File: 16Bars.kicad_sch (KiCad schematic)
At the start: 18 parts, among them J1 3.5mm_Mono_Switched, J2 Conn_02x05_Odd_Even, SW1 SW_Push_LED_Thonk_Low_Profile, SW2 SW_SPDT-EG1249, SW3 SW_SPDT-EG1249

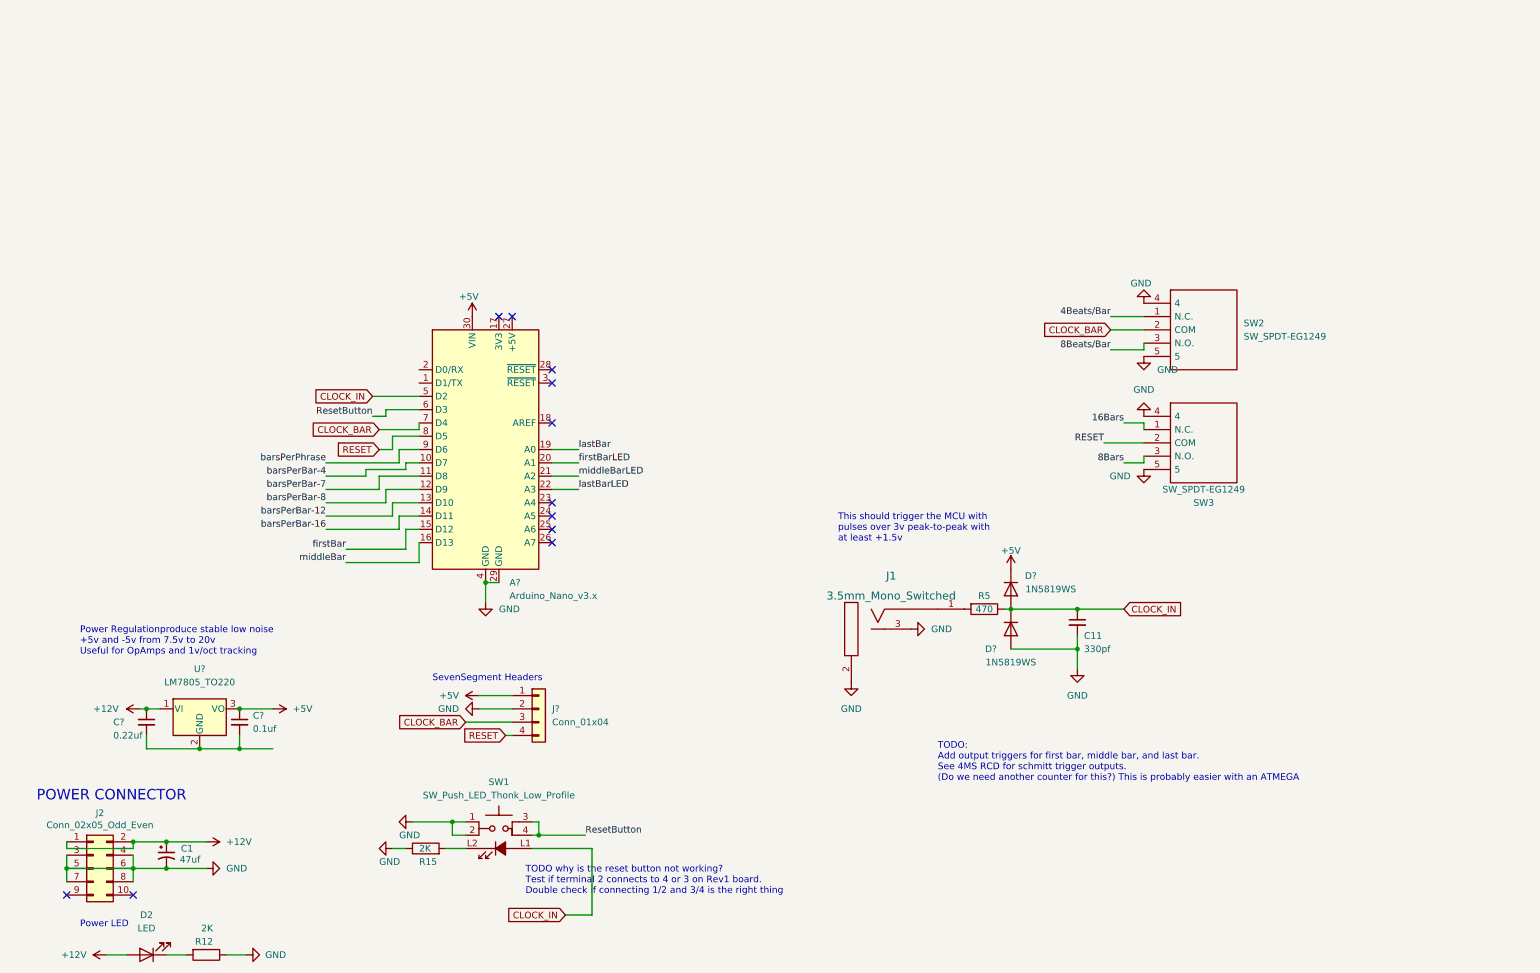
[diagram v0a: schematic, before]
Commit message: Add LCSC power regulator. Add SLB1570 5 position switch.
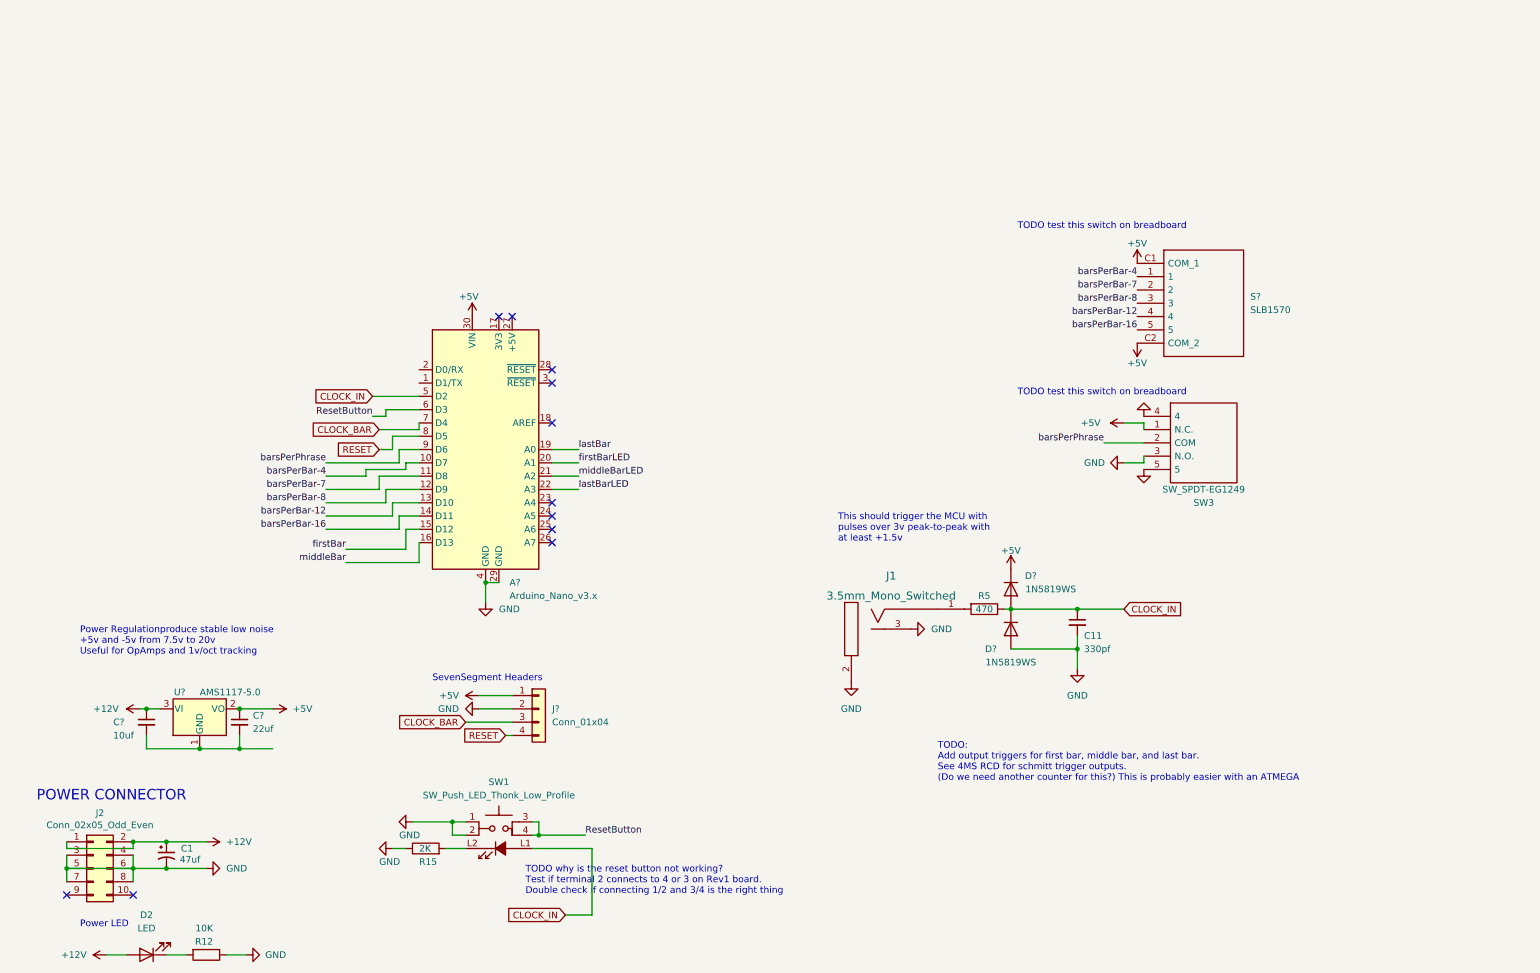
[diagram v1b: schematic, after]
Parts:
- removed SW2: SW_SPDT-EG1249, EG1249, symbol SamacSys_Parts:EG1249-On-On
- added S?: SLB1570, SLB1570, symbol SLB1570:SLB1570
- C?: value 0.1uf -> 22uf
- C?: value 0.22uf -> 10uf
- R12: value 2K -> 10K
- U?: value LM7805_TO220 -> AMS1117-5.0; footprint Package_TO_SOT_THT:TO-220-3_Vertical -> Package_TO_SOT_SMD:SOT-223-3_TabPin2; symbol Regulator_Linear:LM7805_TO220 -> Regulator_Linear:AMS1117-5.0; LCSC (none) -> C6187
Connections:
- net 16Bars is gone; now on net +5V: SW3.1 (N.C.)
- net 8Bars is gone; now on net GND: SW3.3 (N.O.)
- net +12V: now also U?.3 (VI); no longer U?.1 (VI)
- net +5V: now also U?.2 (VO), S?.C1 (COM_1), S?.C2 (COM_2); no longer U?.3 (VO)
- net RESET: no longer SW3.2 (COM)
- net barsPerBar-12: now also S?.4
- net barsPerBar-16: now also S?.5
- net barsPerBar-4: now also S?.1
- net barsPerBar-7: now also S?.2
- net barsPerBar-8: now also S?.3
- net barsPerPhrase: now also SW3.2 (COM)
- net at C?.2, C?.2: now also U?.1 (GND); no longer U?.2 (GND)
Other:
- note added: "TODO test this switch on breadboard"

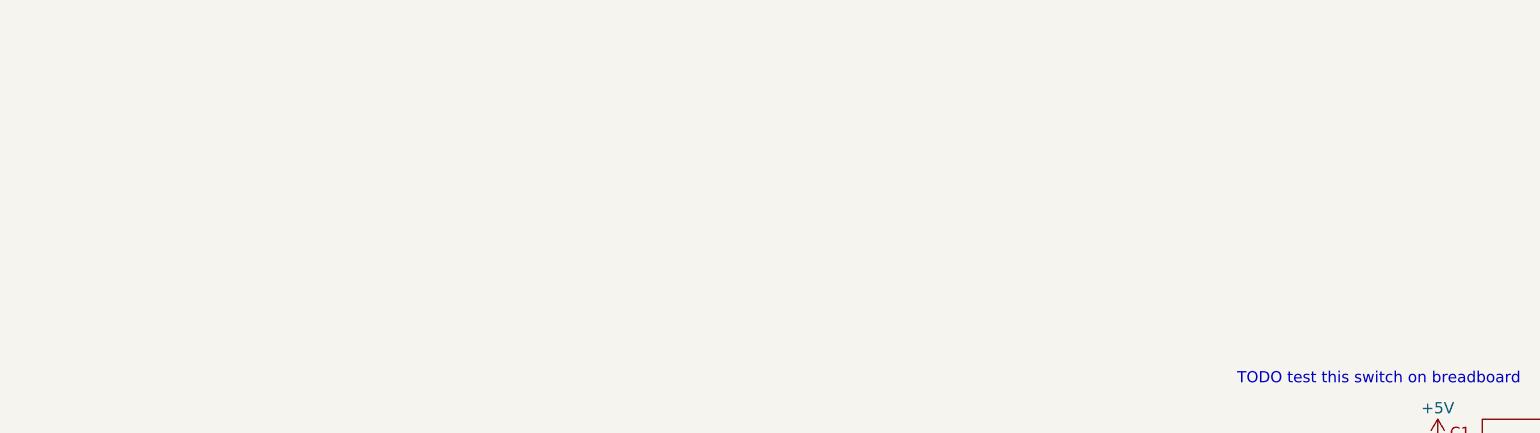
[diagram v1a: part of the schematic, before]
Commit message: Add output jacks and leds.
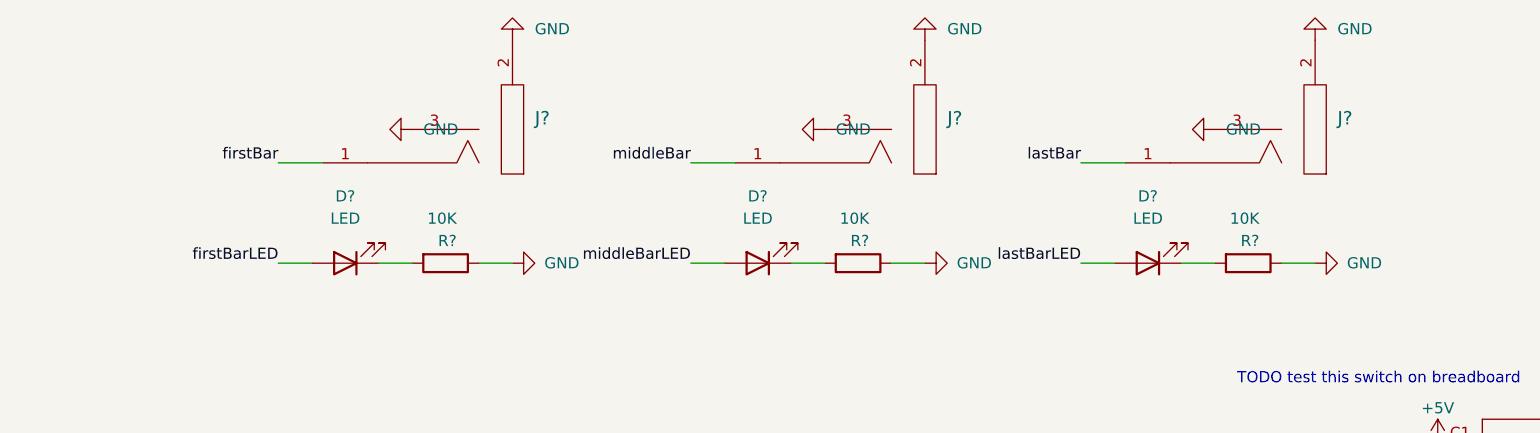
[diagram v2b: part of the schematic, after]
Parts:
- added D? (x3): LED, LED_SMD:LED_0603_1608Metric, symbol Device:LED
- added J? (x3): 3.5mm_Mono_Switched, 4ms_Jack:EighthInch_PJ398SM, symbol 4ms_Jack:3.5mm_Mono_Switched
- added R? (x3): 10K, Resistor_SMD:R_0402_1005Metric, symbol Device:R
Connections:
- net GND: now also J?.2 (SHEILD), J?.2 (SHEILD), J?.2 (SHEILD), J?.3 (SW), J?.3 (SW), J?.3 (SW), R?.1, R?.1, R?.1
- net firstBar: now also J?.1 (SIG)
- net firstBarLED: now also D?.2 (A)
- net lastBar: now also J?.1 (SIG)
- net lastBarLED: now also D?.2 (A)
- net middleBar: now also J?.1 (SIG)
- net middleBarLED: now also D?.2 (A)
- new net: D?.1 (K), R?.2 (x3)

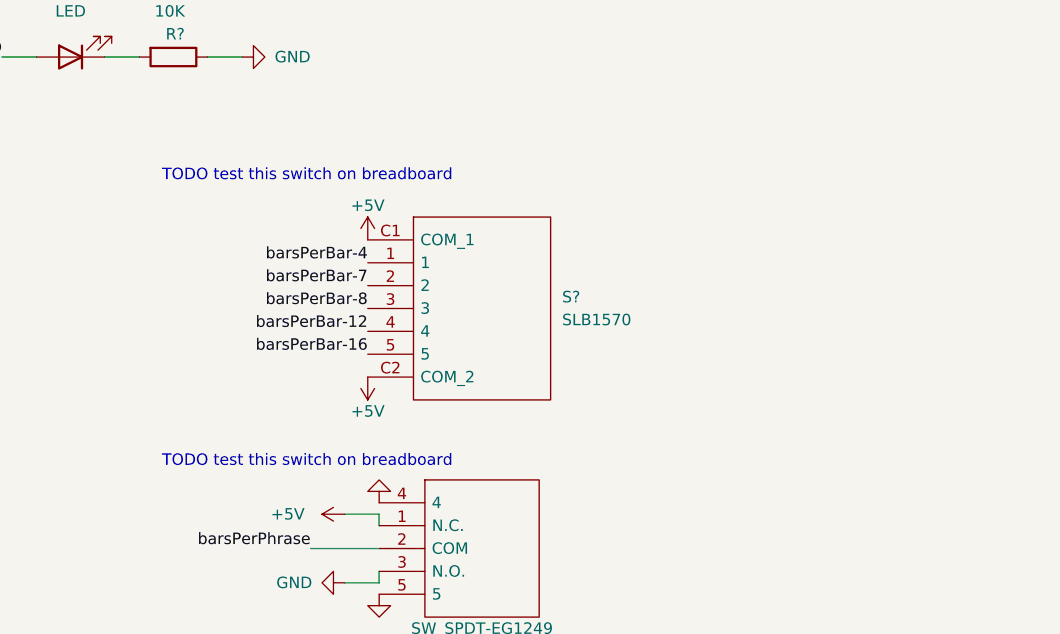
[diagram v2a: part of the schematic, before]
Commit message: Verified 1P5T Switch on Breadboard.
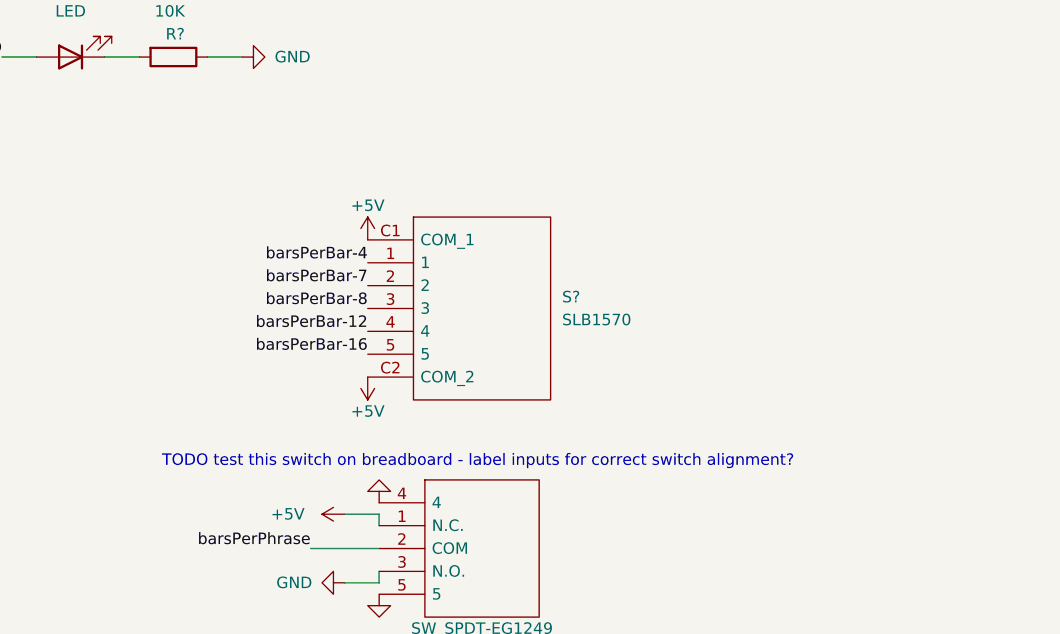
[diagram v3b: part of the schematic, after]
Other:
- note added: "TODO test this switch on breadboard - label inputs for correct switch alignment?"
- note removed: "TODO test this switch on breadboard"
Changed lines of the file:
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@@
     (effects (font (size 2 2)) (justify right bottom))
-  )
-  (text "TODO test this switch on breadboard" (at 204.47 60.96 0)
-    (effects (font (size 1.27 1.27)) (justify left bottom))
   )
   (text "Power LED" (at 25.4 194.31 0)
@@
     (effects (font (size 1.27 1.27)) (justify left bottom))
   )
-  (text "TODO test this switch on breadboard" (at 204.47 92.71 0)
+  (text "TODO test this switch on breadboard - label inputs for correct switch alignment?"
+    (at 204.47 92.71 0)
     (effects (font (size 1.27 1.27)) (justify left bottom))
   )

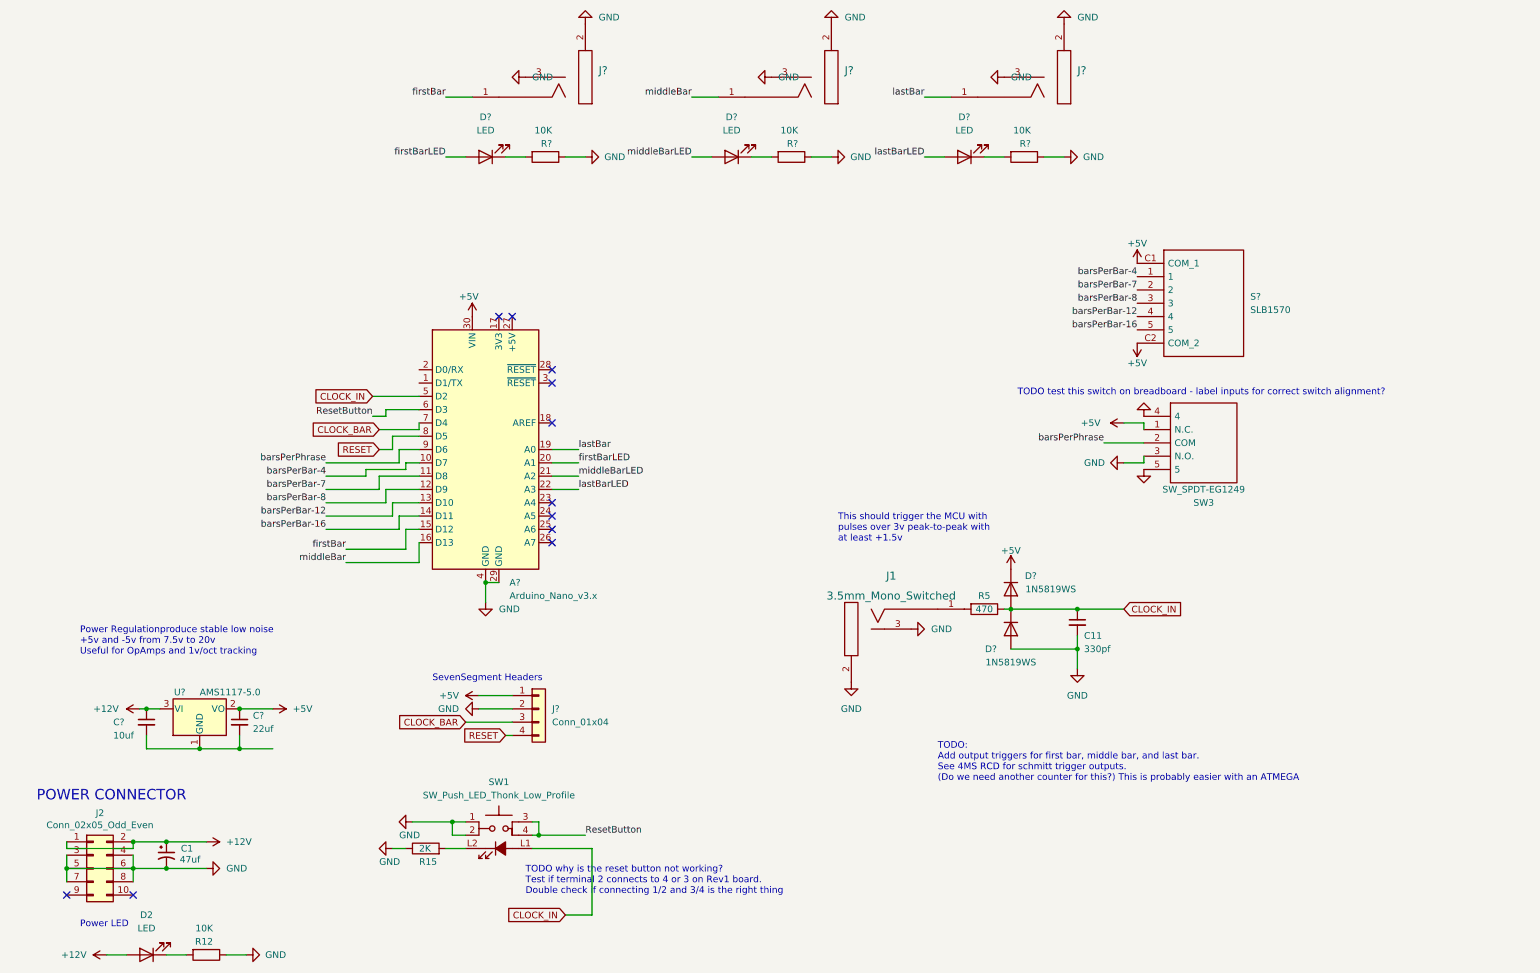
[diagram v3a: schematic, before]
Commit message: Remove AMS1117
Arduino has one onboard!
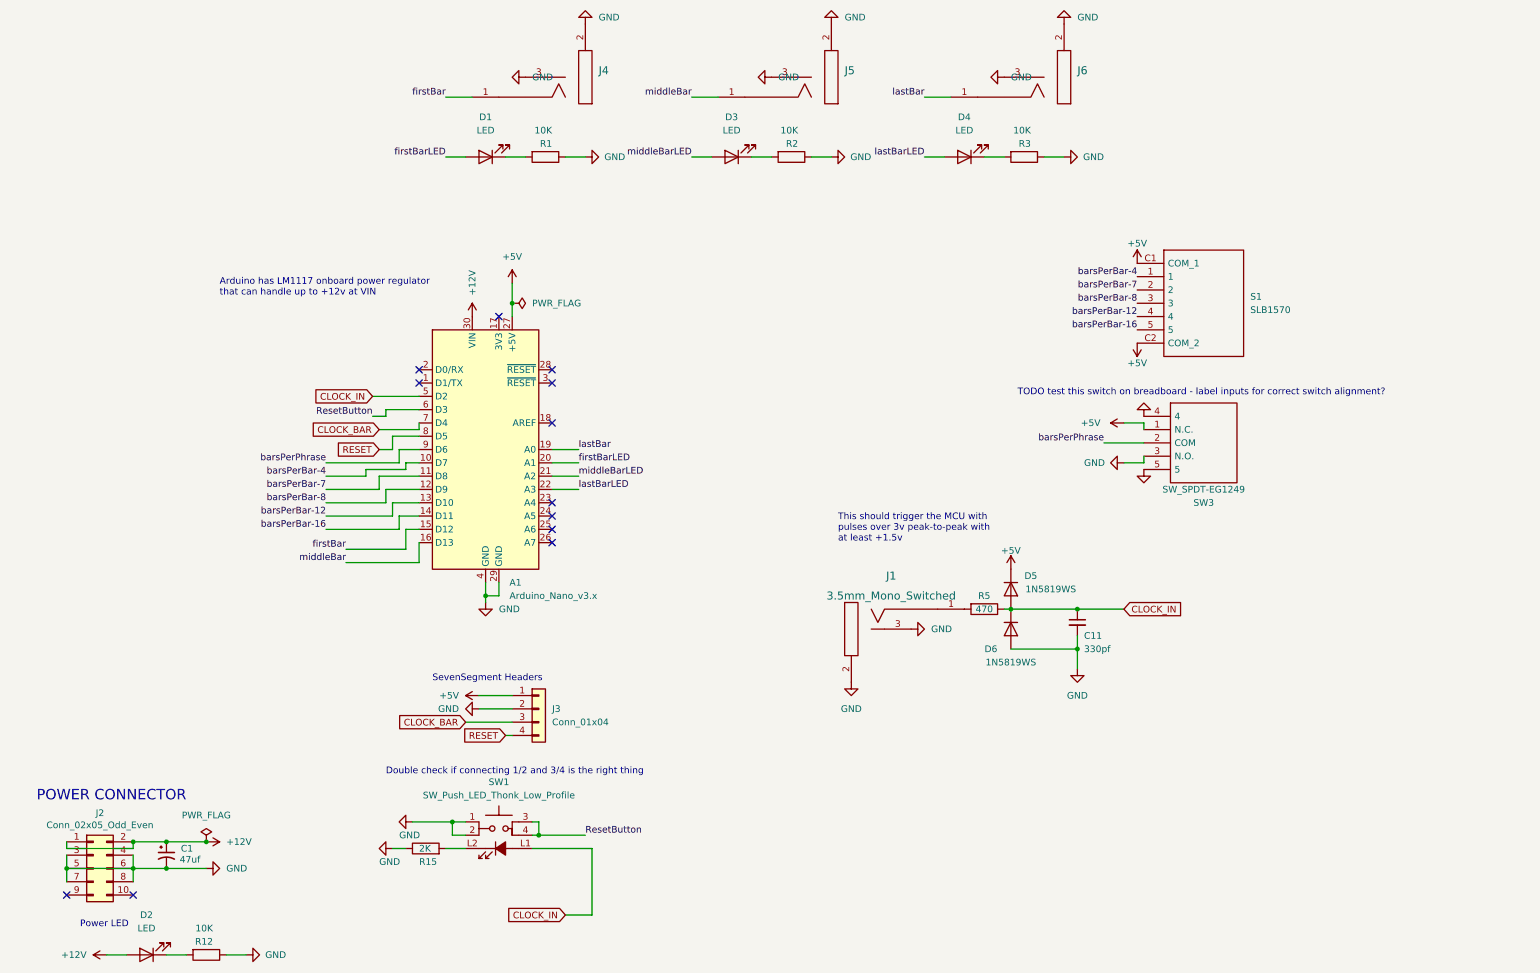
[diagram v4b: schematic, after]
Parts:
- removed C?: 22uf, symbol Device:C_Small
- removed C?: 10uf, symbol Device:C_Small
- removed U?: AMS1117-5.0, Package_TO_SOT_SMD:SOT-223-3_TabPin2, symbol Regulator_Linear:AMS1117-5.0
- gave numbers to parts that had none: 14
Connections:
- net +12V: now also A1.30 (VIN)
- net +5V: now also A1.27 (+5V); no longer A1.30 (VIN)
- no-connect marks 11 -> 12
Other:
- note added: "Arduino has LM1117 onboard power regulator that can handle up to +12v at VIN"
- note added: "Double check if connecting 1/2 and 3/4 is the right thing"
- note removed: "Power Regulationproduce stable low noise +5v and -5v from 7.5v to 20v Useful for OpAmps and 1v/oct tracking"
- note removed: "TODO why is the reset button not working? Test if terminal 2 connects to 4 or 3 on Rev1 board. Double check if connecting 1/2 and 3/4 is the right thing"
- note removed: "TODO: Add output triggers for first bar, middle bar, and last bar. See 4MS RCD for schmitt trigger outputs. (Do we need another counter for this?) This is probably easier with an ATMEGA"
